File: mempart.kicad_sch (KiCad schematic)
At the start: 14 parts, among them U11 SDRAM, U12 SDRAM

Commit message: External I/O
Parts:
- renumbered C413 to C411, C414 to C412, R157 to R139, R149 to R140, R150 to R141, R152 to R142, R151 to R143, R155 to R144, R156 to R145, R153 to R146, R154 to R147, R158 to R148, U11 to U, U12 to U10
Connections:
- net CLK0_DN: no longer R145.2, U10.J10 (CLK_DN)
- net CLK0_DP: no longer R144.2, U10.J11 (CLK_DP)
- net GND: now also U.B10 (DQ9), U.B11 (DQ8), U.B2 (DQ0), U.B3 (DQ1), U.C11 (DQ10), U.C3 (DQ3), U.E11 (DQ12), U.E2 (DQ4), U.F10 (DQ13), U.F11 (DQ14), U.F2 (DQ6), U.F3 (DQ5), U.G10 (DQ15), U.G3 (DQ7), U.L10 (DQ17), U.L3 (DQ25), U.M10 (DQ19), U.M11 (DQ16), U.M2 (DQ24), U.M3 (DQ27), U.N11 (DQ18), U.N2 (DQ26), U.R10 (DQ21), U.R11 (DQ20), U.R2 (DQ28), U.R3 (DQ29), U.T10 (DQ23), U.T11 (DQ22), U.T2 (DQ30), U.T3 (DQ31); no longer U.A10 (VSS2), U.A3 (VSS0), U.B1 (VSSQ0), U.B12 (VSSQ3), U.B4 (VSSQ1), U.B9 (VSSQ2), U.D1 (VSSQ4), U.D12 (VSSQ7), U.D4 (VSSQ5), U.D9 (VSSQ6), U.G1 (VSS3), U.G11 (VSSQ9), U.G12 (VSS4), U.G2 (VSSQ8), U.J1 (VSSA0), U.J12 (VSSA1), U.L1 (VSS5), U.L11 (VSSQ11), U.L12 (VSS6), U.L2 (VSSQ10), U.P1 (VSSQ12), U.P12 (VSSQ15), U.P4 (VSSQ13), U.P9 (VSSQ14), U.T1 (VSSQ16), U.T12 (VSSQ19), U.T4 (VSSQ17), U.T9 (VSSQ18), U.V10 (VSS1), U.V3 (VSS7)
- net V_MEM: now also U.A9 (MF), U.F4 (CAS_N), U.F9 (CS_N), U.G4 (BA0), U.G9 (BA1), U.H10 (BA2), U.H11 (A5), U.H2 (A1), U.H3 (RAS_N), U.H9 (WE_N), U.J10 (CLK_DN), U.J11 (CLK_DP), U.J2 (A12), U.J3 (CS1_N), U.K10 (A6), U.K11 (A8), U.K2 (A10), U.K3 (A2), U.K4 (A0), U.K9 (A4), U.L4 (A11), U.L9 (A7), U.M4 (A3), U.M9 (A9), U.P11 (WDQS2), U.P2 (WDQS3), U.V4 (SCAN_EN), U.V9 (RESET); no longer U.A1 (VDDQ0), U.A11 (VDD1), U.A12 (VDDQ1), U.A2 (VDD0), U.C1 (VDDQ2), U.C12 (VDDQ5), U.C4 (VDDQ3), U.C9 (VDDQ4), U.E1 (VDDQ6), U.E12 (VDDQ9), U.E4 (VDDQ7), U.E9 (VDDQ8), U.F1 (VDD2), U.F12 (VDD3), U.J4 (VDDQ10), U.J9 (VDDQ11), U.K1 (VDDA0), U.K12 (VDDA1), U.M1 (VDD5), U.M12 (VDD6), U.N1 (VDDQ12), U.N12 (VDDQ16), U.N4 (VDDQ13), U.N9 (VDDQ15), U.R1 (VDDQ17), U.R12 (VDDQ20), U.R4 (VDDQ18), U.R9 (VDDQ19), U.V1 (VDDQ21), U.V11 (VDD4), U.V12 (VDDQ14), U.V2 (VDD7)
- net at R139.1: now also U.P3 (RDQS3); no longer U.A4 (ZQ)
- new net CLK1_DN: R145.2, U10.J10 (CLK_DN)
- new net CLK1_DP: R144.2, U10.J11 (CLK_DP)
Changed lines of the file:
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@@
 		)
 	)
-	(label "CLK0_DP"
+	(label "CLK1_DP"
 		(at 171.45 153.67 180)
 		(effects
@@
 		)
 	)
-	(label "CLK0_DN"
+	(label "CLK1_DN"
 		(at 171.45 156.21 180)
 		(effects
@@
 		(on_board yes)
 		(dnp no)
-		(property "Reference" "#PWR0323"
+		(property "Reference" "#PWR0312"
 			(at 67.31 209.55 0)
 			(effects
@@
 		(dnp no)
 		(fields_autoplaced yes)
-		(property "Reference" "#PWR0322"
+		(property "Reference" "#PWR0307"
 			(at 67.31 196.85 0)
 			(effects
@@
 		(lib_id "SDRAM:SDRAM")
 		(at 203.2 86.36 0)
-		(unit 2)
+		(unit 1)
 		(exclude_from_sim no)
 		(in_bom yes)
@@
 		(dnp no)
 		(fields_autoplaced yes)
-		(property "Reference" "U11"
+		(property "Reference" "U"
 			(at 203.2 26.67 0)
 			(effects
@@
 		(dnp no)
 		(fields_autoplaced yes)
-		(property "Reference" "#PWR0324"
+		(property "Reference" "#PWR0313"
 			(at 67.31 232.41 0)
 			(effects
@@
 		(on_board yes)
 		(dnp no)
-		(property "Reference" "#PWR0327"
+		(property "Reference" "#PWR0301"
 			(at 168.91 36.83 0)
 			(effects
@@
 		(dnp no)
 		(fields_autoplaced yes)
-		(property "Reference" "#PWR0331"
+		(property "Reference" "#PWR0315"
 			(at 351.79 233.68 0)
 			(effects
@@
 		(on_board yes)
 		(dnp no)
-		(property "Reference" "C414"
+		(property "Reference" "C412"
 			(at 59.69 220.98 0)
 			(effects
@@
 		(on_board yes)
 		(dnp no)
-		(property "Reference" "R158"
+		(property "Reference" "R148"
 			(at 360.934 229.87 0)
 			(effects
@@
 		(dnp no)
 		(fields_autoplaced yes)
-		(property "Reference" "U12"
+		(property "Reference" "U10"
 			(at 317.5 132.08 0)
 			(effects
@@
 		(on_board yes)
 		(dnp no)
-		(property "Reference" "R151"
+		(property "Reference" "R143"
 			(at 68.834 172.72 0)
 			(effects
@@
 		(dnp no)
 		(fields_autoplaced yes)
-		(property "Reference" "#PWR0329"
+		(property "Reference" "#PWR0303"
 			(at 245.11 135.89 0)
 			(effects
@@
 		(dnp no)
 		(fields_autoplaced yes)
-		(property "Reference" "#PWR0320"
+		(property "Reference" "#PWR0311"
 			(at 57.15 232.41 0)
 			(effects
@@
 		(on_board yes)
 		(dnp no)
-		(property "Reference" "R156"
+		(property "Reference" "R145"
 			(at 162.814 146.05 0)
 			(effects
@@
 		(on_board yes)
 		(dnp no)
-		(property "Reference" "#PWR0330"
+		(property "Reference" "#PWR0314"
 			(at 283.21 142.24 0)
 			(effects
@@
 		(on_board yes)
 		(dnp no)
-		(property "Reference" "R153"
+		(property "Reference" "R146"
 			(at 68.834 208.28 0)
 			(effects
@@
 		(on_board yes)
 		(dnp no)
-		(property "Reference" "R157"
+		(property "Reference" "R139"
 			(at 246.634 124.46 0)
 			(effects
@@
 		(on_board yes)
 		(dnp no)
-		(property "Reference" "#PWR0325"
+		(property "Reference" "#PWR0309"
 			(at 151.13 147.32 0)
 			(effects
@@
 		(dnp no)
 		(fields_autoplaced yes)
-		(property "Reference" "U11"
+		(property "Reference" "U"
 			(at 88.9 39.37 0)
 			(effects
@@
 		(on_board yes)
 		(dnp no)
-		(property "Reference" "R155"
+		(property "Reference" "R144"
 			(at 152.654 146.05 0)
 			(effects
@@
 		(on_board yes)
 		(dnp no)
-		(property "Reference" "R150"
+		(property "Reference" "R141"
 			(at 48.514 40.64 0)
 			(effects
@@
 		(on_board yes)
 		(dnp no)
-		(property "Reference" "#PWR0321"
+		(property "Reference" "#PWR0308"
 			(at 67.31 173.99 0)
 			(effects
@@
 		(dnp no)
 		(fields_autoplaced yes)
-		(property "Reference" "#PWR0328"
+		(property "Reference" "#PWR"
 			(at 237.49 128.27 0)
 			(effects
@@
 		(dnp no)
 		(fields_autoplaced yes)
-		(property "Reference" "#PWR0332"
+		(property "Reference" "#PWR0316"
 			(at 359.41 241.3 0)
 			(effects
@@
 		(dnp no)
 		(fields_autoplaced yes)
-		(property "Reference" "U12"
+		(property "Reference" "U10"
 			(at 203.2 144.78 0)
 			(effects
@@
 		(on_board yes)
 		(dnp no)
-		(property "Reference" "#PWR0317"
+		(property "Reference" "#PWR0304"
 			(at 36.83 41.91 0)
 			(effects
@@
 		(on_board yes)
 		(dnp no)
-		(property "Reference" "#PWR0318"
+		(property "Reference" "#PWR0305"
 			(at 46.99 41.91 0)
 			(effects
@@
 		(dnp no)
 		(fields_autoplaced yes)
-		(property "Reference" "#PWR0319"
+		(property "Reference" "#PWR"
 			(at 57.15 196.85 0)
 			(effects
@@
 		(on_board yes)
 		(dnp no)
-		(property "Reference" "R154"
+		(property "Reference" "R147"
 			(at 68.834 220.98 0)
 			(effects
@@
 		(on_board yes)
 		(dnp no)
-		(property "Reference" "#PWR0326"
+		(property "Reference" "#PWR0310"
 			(at 161.29 147.32 0)
 			(effects
@@
 		(on_board yes)
 		(dnp no)
-		(property "Reference" "R149"
+		(property "Reference" "R140"
 			(at 38.354 40.64 0)
 			(effects
@@
 		(on_board yes)
 		(dnp no)
-		(property "Reference" "C413"
+		(property "Reference" "C411"
 			(at 59.69 185.42 0)
 			(effects
@@
 		(on_board yes)
 		(dnp no)
-		(property "Reference" "R152"
+		(property "Reference" "R142"
 			(at 68.834 185.42 0)
 			(effects

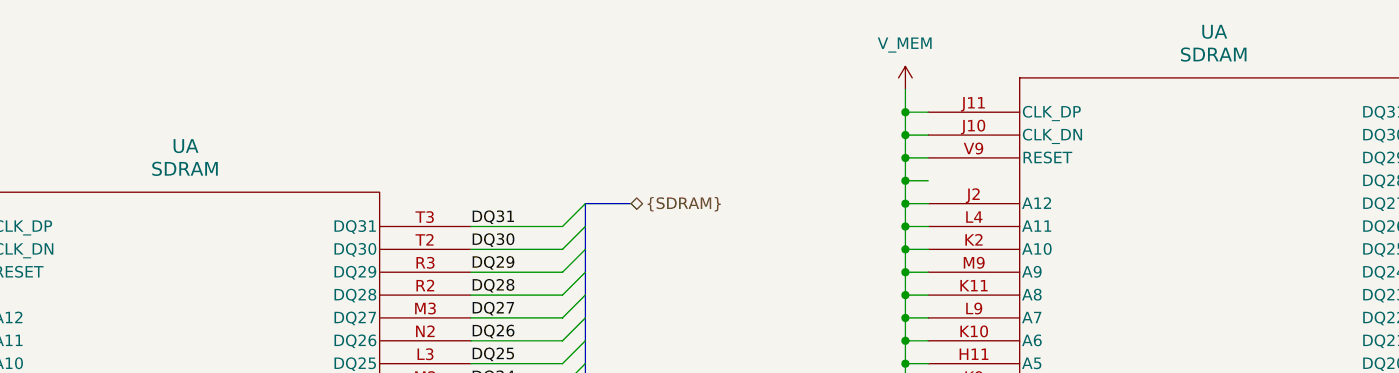
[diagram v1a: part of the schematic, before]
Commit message: Cleanup, SMC GPIO connections and Temperature sensing
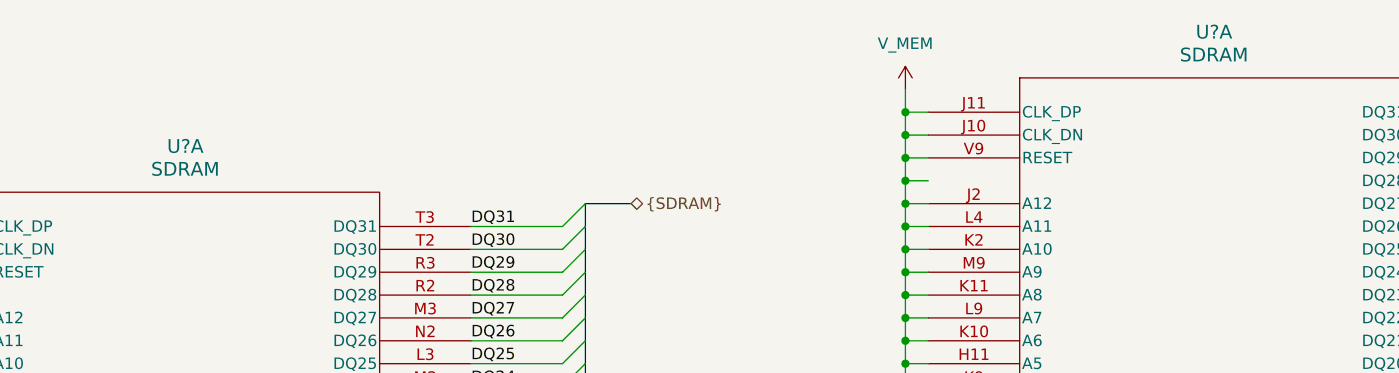
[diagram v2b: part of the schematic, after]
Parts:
- renumbered U to U?
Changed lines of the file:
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@@
 		(dnp no)
 		(fields_autoplaced yes)
-		(property "Reference" "U"
+		(property "Reference" "U?"
 			(at 203.2 26.67 0)
 			(effects
@@
 		(instances
 			(project "Mantaray"
+				(path "/16640ecb-e4a4-4594-871b-70047bfba6e0/3ac4cd05-2682-4faa-958d-341ea57a54eb/07e21cc7-5b84-4539-a1a8-41dc855ac572"
+					(reference "U?")
+					(unit 1)
+				)
 				(path "/16640ecb-e4a4-4594-871b-70047bfba6e0/3ac4cd05-2682-4faa-958d-341ea57a54eb/605d31e7-44df-42ff-9e2e-ced6c62f08fe"
 					(reference "U15")
@@
 		(dnp no)
 		(fields_autoplaced yes)
-		(property "Reference" "U"
+		(property "Reference" "U?"
 			(at 88.9 39.37 0)
 			(effects
@@
 		(instances
 			(project "Mantaray"
+				(path "/16640ecb-e4a4-4594-871b-70047bfba6e0/3ac4cd05-2682-4faa-958d-341ea57a54eb/07e21cc7-5b84-4539-a1a8-41dc855ac572"
+					(reference "U?")
+					(unit 1)
+				)
 				(path "/16640ecb-e4a4-4594-871b-70047bfba6e0/3ac4cd05-2682-4faa-958d-341ea57a54eb/605d31e7-44df-42ff-9e2e-ced6c62f08fe"
 					(reference "U15")
@@
 		(dnp no)
 		(fields_autoplaced yes)
-		(property "Reference" "#PWR"
+		(property "Reference" "#PWR?"
 			(at 237.49 128.27 0)
 			(effects
@@
 		(instances
 			(project "Mantaray"
+				(path "/16640ecb-e4a4-4594-871b-70047bfba6e0/3ac4cd05-2682-4faa-958d-341ea57a54eb/07e21cc7-5b84-4539-a1a8-41dc855ac572"
+					(reference "#PWR?")
+					(unit 1)
+				)
 				(path "/16640ecb-e4a4-4594-871b-70047bfba6e0/3ac4cd05-2682-4faa-958d-341ea57a54eb/605d31e7-44df-42ff-9e2e-ced6c62f08fe"
 					(reference "#PWR0360")
@@
 		(dnp no)
 		(fields_autoplaced yes)
-		(property "Reference" "#PWR"
+		(property "Reference" "#PWR?"
 			(at 57.15 196.85 0)
 			(effects
@@
 		(instances
 			(project "Mantaray"
+				(path "/16640ecb-e4a4-4594-871b-70047bfba6e0/3ac4cd05-2682-4faa-958d-341ea57a54eb/07e21cc7-5b84-4539-a1a8-41dc855ac572"
+					(reference "#PWR?")
+					(unit 1)
+				)
 				(path "/16640ecb-e4a4-4594-871b-70047bfba6e0/3ac4cd05-2682-4faa-958d-341ea57a54eb/605d31e7-44df-42ff-9e2e-ced6c62f08fe"
 					(reference "#PWR0351")

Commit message: Internal Connectors
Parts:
- removed U?: SDRAM, symbol SDRAM:SDRAM
- added unit 2 of U5
- gave numbers to parts that had none: 1
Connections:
- net GND: now also U5.A10 (VSS2), U5.A3 (VSS0), U5.B1 (VSSQ0), U5.B12 (VSSQ3), U5.B4 (VSSQ1), U5.B9 (VSSQ2), U5.D1 (VSSQ4), U5.D12 (VSSQ7), U5.D4 (VSSQ5), U5.D9 (VSSQ6), U5.G1 (VSS3), U5.G11 (VSSQ9), U5.G12 (VSS4), U5.G2 (VSSQ8), U5.J1 (VSSA0), U5.J12 (VSSA1), U5.L1 (VSS5), U5.L11 (VSSQ11), U5.L12 (VSS6), U5.L2 (VSSQ10), U5.P1 (VSSQ12), U5.P12 (VSSQ15), U5.P4 (VSSQ13), U5.P9 (VSSQ14), U5.T1 (VSSQ16), U5.T12 (VSSQ19), U5.T4 (VSSQ17), U5.T9 (VSSQ18), U5.V10 (VSS1), U5.V3 (VSS7)
- net V_MEM: now also U5.A1 (VDDQ0), U5.A11 (VDD1), U5.A12 (VDDQ1), U5.A2 (VDD0), U5.C1 (VDDQ2), U5.C12 (VDDQ5), U5.C4 (VDDQ3), U5.C9 (VDDQ4), U5.E1 (VDDQ6), U5.E12 (VDDQ9), U5.E4 (VDDQ7), U5.E9 (VDDQ8), U5.F1 (VDD2), U5.F12 (VDD3), U5.J4 (VDDQ10), U5.J9 (VDDQ11), U5.K1 (VDDA0), U5.K12 (VDDA1), U5.M1 (VDD5), U5.M12 (VDD6), U5.N1 (VDDQ12), U5.N12 (VDDQ16), U5.N4 (VDDQ13), U5.N9 (VDDQ15), U5.R1 (VDDQ17), U5.R12 (VDDQ20), U5.R4 (VDDQ18), U5.R9 (VDDQ19), U5.V1 (VDDQ21), U5.V11 (VDD4), U5.V12 (VDDQ14), U5.V2 (VDD7)
- net at R139.1: now also U5.A4 (ZQ)

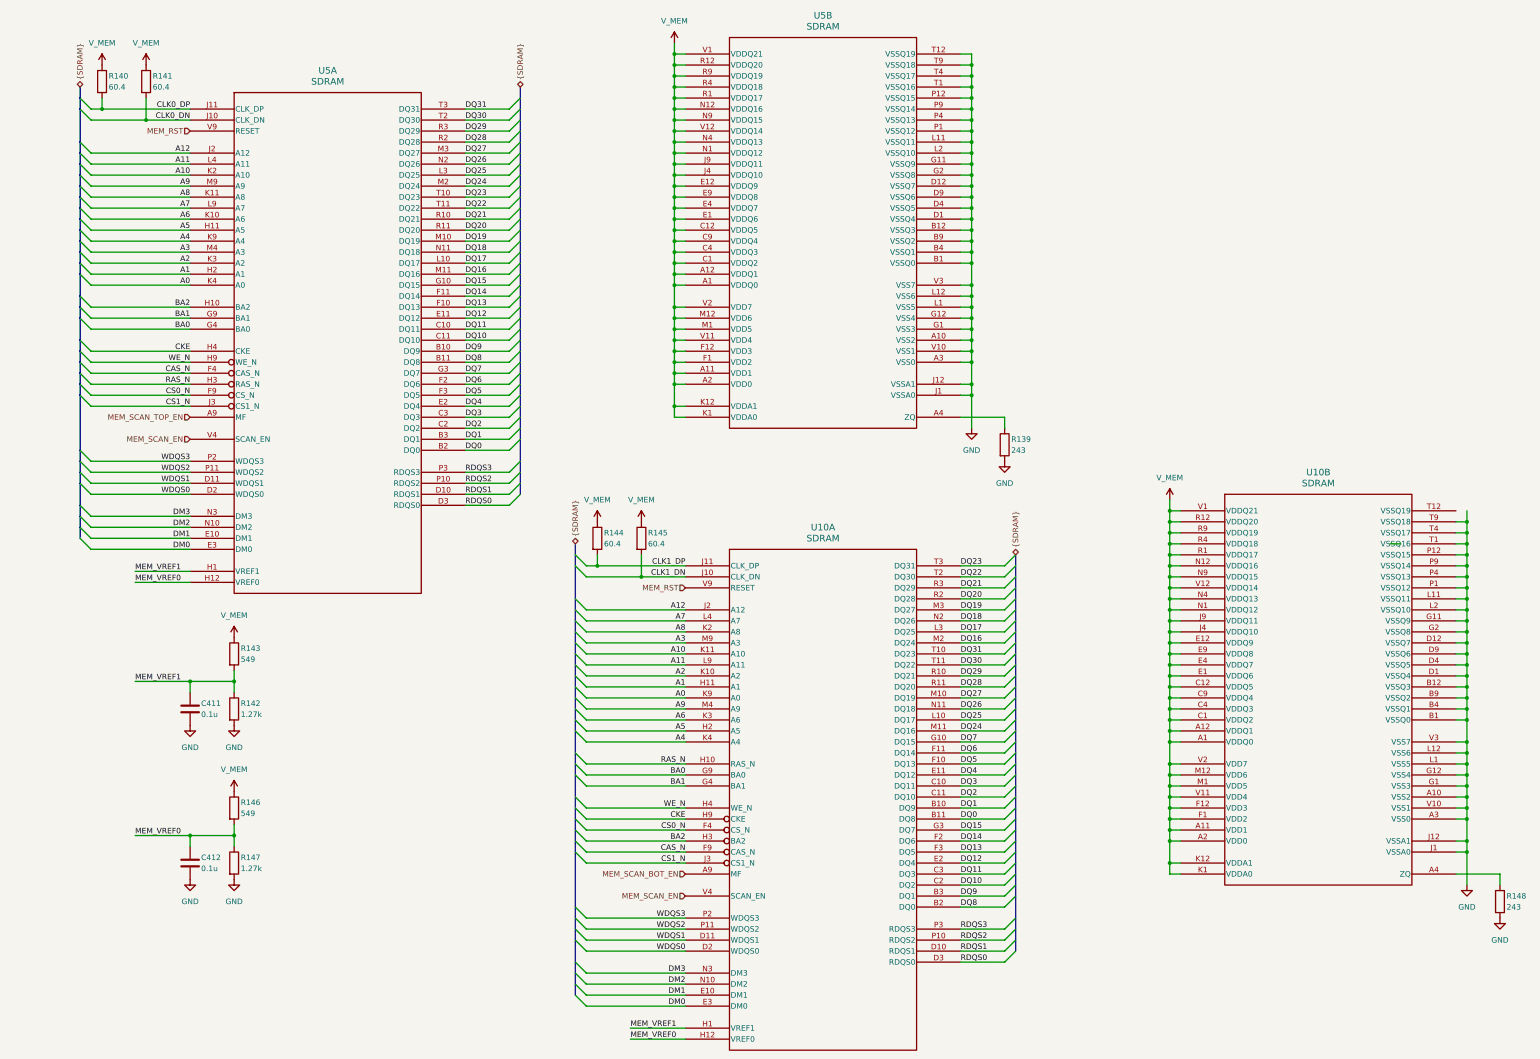
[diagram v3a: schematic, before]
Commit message: Multipurpose and standby power rails, Reannotated schematic
Added V_1P2, V_1P8, V_5P0DUAL, V_EFUSE, V_GPUPCIE, V_3P3STBY and V_1P2STBY
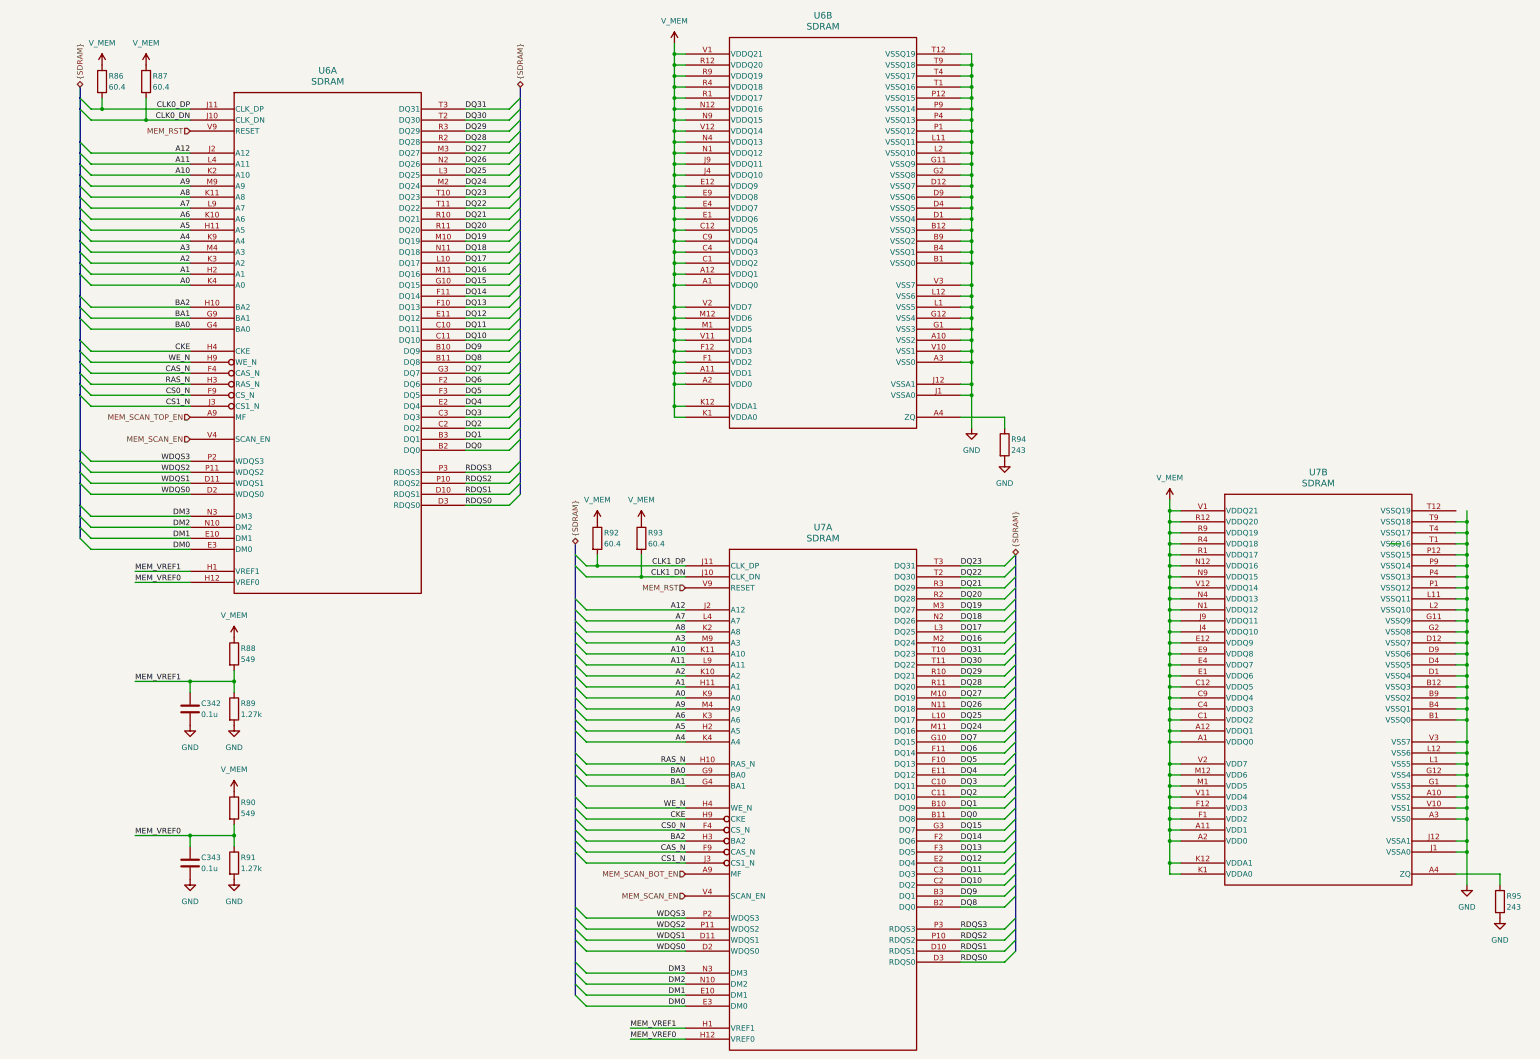
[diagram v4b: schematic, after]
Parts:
- renumbered C411 to C342, C412 to C343, R140 to R86, R141 to R87, R143 to R88, R142 to R89, R146 to R90, R147 to R91, R144 to R92, R145 to R93, R139 to R94, R148 to R95, U5 to U6, U10 to U7
